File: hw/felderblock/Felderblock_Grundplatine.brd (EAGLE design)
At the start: 100 x 78 mm, 54 parts, among them IC2 LM2936, IC3 ULN2803, IC4 MCP2300X/P, J1 RJ11, J2 RJ11, M1 ARDUINO-NANO-3.0, T2 BC337, X1 TASTENSPERRE1, X2 TASTENSPERRE2, X3 SCHL-SPERRE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

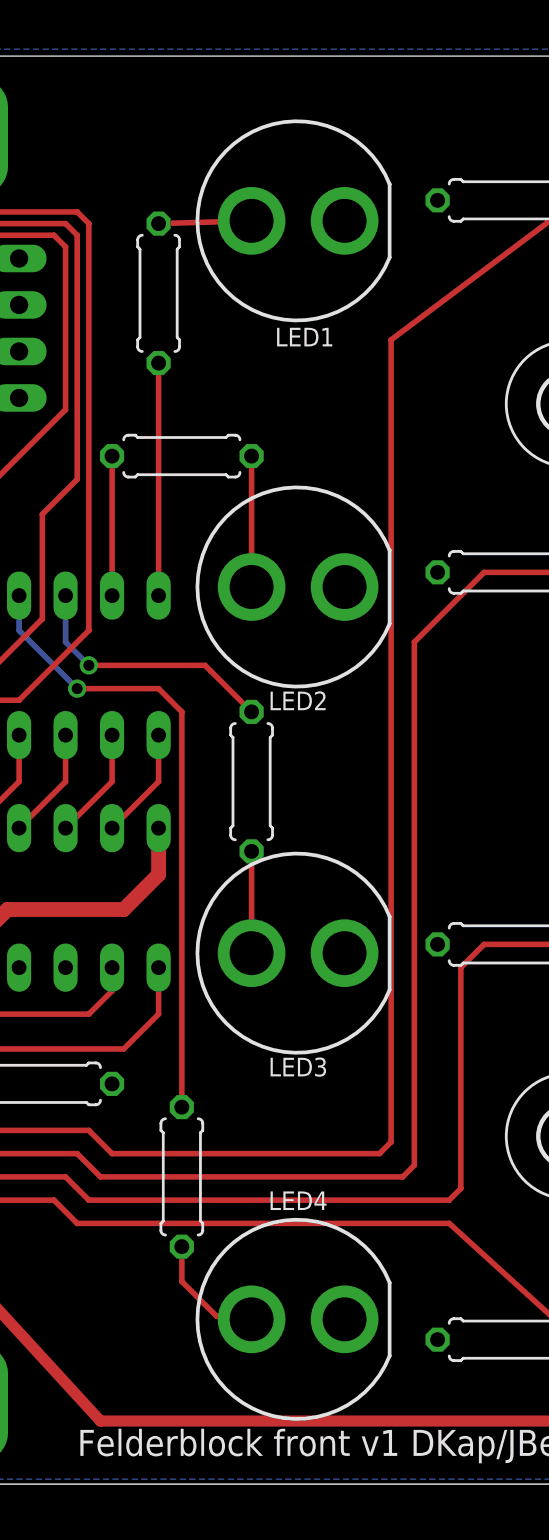
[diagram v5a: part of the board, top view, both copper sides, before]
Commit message: LED 10mm updated
changes:
- footprint 10mm LED
- INT not connected to GND (=output)
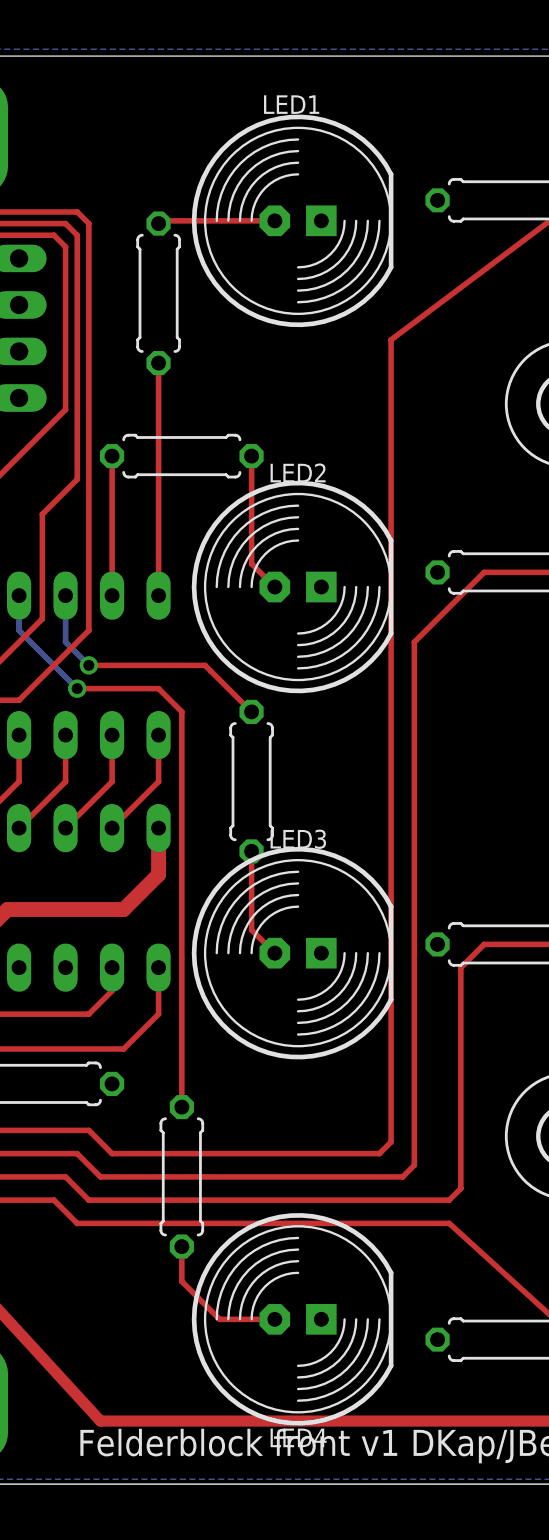
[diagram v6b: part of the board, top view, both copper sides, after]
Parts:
- LED1, LED2, LED3, LED4: device SparkFun-LED:LED_10MM -> led:LED10MM
- turned LED1 to 0 degrees
- turned LED2 to 0 degrees
- turned LED3 to 0 degrees
- turned LED4 to 0 degrees
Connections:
- removed net N$19: IC3.8
- removed net N$27: IC3.11
- net GND: now also LED1.K, LED2.K, LED3.K, LED4.K; no longer IC4.8, LED1.C, LED2.C, LED3.C, LED4.C
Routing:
- net N$4: track 5.08 -> 6.41 mm
- net N$9: track 6.51 -> 7.84 mm
- net N$8: track 5.56 -> 6.09 mm
- net N$5: track 7.15 -> 7.68 mm
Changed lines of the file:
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@@
 <attribute name="SF_ID" value="PRT_10877" x="6.35" y="54.61" size="1.778" layer="28" rot="MR0" display="off"/>
 </element>
-<element name="LED1" library="SparkFun-LED" package="LED_10MM" value="" x="76.2" y="70" smashed="yes" rot="R180">
-<attribute name="NAME" x="74.93" y="63.65" size="1.016" layer="25" ratio="20" rot="R180" align="center-right"/>
-<attribute name="VALUE" x="76.2" y="75.715" size="0.6096" layer="27" font="vector" ratio="20" rot="R180" align="top-center"/>
-</element>
-<element name="LED2" library="SparkFun-LED" package="LED_10MM" value="" x="76.2" y="50" smashed="yes" rot="R180">
-<attribute name="NAME" x="76.2" y="44.285" size="1.016" layer="25" ratio="20" rot="R180" align="bottom-center"/>
-<attribute name="VALUE" x="76.2" y="55.715" size="0.6096" layer="27" font="vector" ratio="20" rot="R180" align="top-center"/>
-</element>
-<element name="LED3" library="SparkFun-LED" package="LED_10MM" value="" x="76.2" y="30" smashed="yes" rot="R180">
-<attribute name="NAME" x="76.2" y="24.285" size="1.016" layer="25" ratio="20" rot="R180" align="bottom-center"/>
-<attribute name="VALUE" x="76.2" y="35.715" size="0.6096" layer="27" font="vector" ratio="20" rot="R180" align="top-center"/>
-</element>
-<element name="LED4" library="SparkFun-LED" package="LED_10MM" value="" x="76.2" y="10" smashed="yes" rot="R180">
-<attribute name="NAME" x="76.2" y="16.985" size="1.016" layer="25" ratio="20" rot="R180" align="bottom-center"/>
-<attribute name="VALUE" x="76.2" y="15.715" size="0.6096" layer="27" font="vector" ratio="20" rot="R180" align="top-center"/>
+<element name="LED1" library="led" package="LED10MM" value="" x="76.2" y="70" smashed="yes">
+<attribute name="NAME" x="77.47" y="76.35" size="1.016" layer="25" ratio="20" align="center-right"/>
+<attribute name="VALUE" x="76.2" y="64.285" size="0.6096" layer="27" font="vector" ratio="20" align="top-center"/>
+</element>
+<element name="LED2" library="led" package="LED10MM" value="" x="76.2" y="50" smashed="yes">
+<attribute name="NAME" x="76.2" y="55.715" size="1.016" layer="25" ratio="20" align="bottom-center"/>
+<attribute name="VALUE" x="76.2" y="44.285" size="0.6096" layer="27" font="vector" ratio="20" align="top-center"/>
+</element>
+<element name="LED3" library="led" package="LED10MM" value="" x="76.2" y="30" smashed="yes">
+<attribute name="NAME" x="76.2" y="35.715" size="1.016" layer="25" ratio="20" align="bottom-center"/>
+<attribute name="VALUE" x="76.2" y="24.285" size="0.6096" layer="27" font="vector" ratio="20" align="top-center"/>
+</element>
+<element name="LED4" library="led" package="LED10MM" value="" x="76.2" y="10" smashed="yes">
+<attribute name="NAME" x="76.2" y="3.015" size="1.016" layer="25" ratio="20" align="bottom-center"/>
+<attribute name="VALUE" x="76.2" y="4.285" size="0.6096" layer="27" font="vector" ratio="20" align="top-center"/>
 </element>
 <element name="M1" library="diy-modules" package="ARDUINO-NANO-3.0" value="ARDUINO-NANO-3.0" x="35.56" y="34.29" smashed="yes" rot="MR90"/>
@@
 <contactref element="R8" pad="2"/>
 <contactref element="R7" pad="2"/>
-<contactref element="LED4" pad="C"/>
-<contactref element="LED3" pad="C"/>
-<contactref element="LED2" pad="C"/>
-<contactref element="LED1" pad="C"/>
+<contactref element="LED4" pad="K"/>
+<contactref element="LED3" pad="K"/>
+<contactref element="LED2" pad="K"/>
+<contactref element="LED1" pad="K"/>
 <contactref element="J3" pad="6"/>
 <contactref element="J3" pad="1"/>
@@
 <contactref element="IC4" pad="9"/>
 <contactref element="IC4" pad="6"/>
-<contactref element="IC4" pad="8"/>
 <wire x1="15.24" y1="71.12" x2="22.86" y2="71.12" width="0.6096" layer="1"/>
 <contactref element="I2C" pad="4"/>
@@
 <contactref element="R11" pad="2"/>
 <contactref element="LED1" pad="A"/>
-<wire x1="68.58" y1="69.85" x2="73.66" y2="70" width="0.3048" layer="1"/>
+<wire x1="74.93" y1="70" x2="68.73" y2="70" width="0.3048" layer="1"/>
+<wire x1="68.73" y1="70" x2="68.58" y2="69.85" width="0.3048" layer="1"/>
 </signal>
 <signal name="N$5">
 <contactref element="R12" pad="2"/>
 <contactref element="LED2" pad="A"/>
-<wire x1="73.66" y1="50" x2="73.66" y2="57.15" width="0.3048" layer="1"/>
+<wire x1="73.66" y1="57.15" x2="73.66" y2="51.27" width="0.3048" layer="1"/>
+<wire x1="73.66" y1="51.27" x2="74.93" y2="50" width="0.3048" layer="1"/>
 </signal>
 <signal name="N$8">
 <contactref element="R13" pad="2"/>
 <contactref element="LED3" pad="A"/>
-<wire x1="73.66" y1="30" x2="73.66" y2="35.56" width="0.3048" layer="1"/>
+<wire x1="73.66" y1="35.56" x2="73.66" y2="31.27" width="0.3048" layer="1"/>
+<wire x1="73.66" y1="31.27" x2="74.93" y2="30" width="0.3048" layer="1"/>
 </signal>
 <signal name="N$9">
@@
 <contactref element="LED4" pad="A"/>
 <wire x1="69.85" y1="13.97" x2="69.85" y2="12.065" width="0.3048" layer="1"/>
-<wire x1="69.85" y1="12.065" x2="71.755" y2="10.16" width="0.3048" layer="1"/>
-<wire x1="71.755" y1="10.16" x2="73.66" y2="10" width="0.3048" layer="1"/>
+<wire x1="74.93" y1="10" x2="71.915" y2="10" width="0.3048" layer="1"/>
+<wire x1="71.915" y1="10" x2="69.85" y2="12.065" width="0.3048" layer="1"/>
 </signal>
 <signal name="FELD1_LED">
@@
 <wire x1="46.99" y1="65.405" x2="43.18" y2="65.405" width="0.3048" layer="1"/>
 </signal>
-<signal name="N$19">
-<contactref element="IC3" pad="8"/>
-</signal>
-<signal name="N$27">
-<contactref element="IC3" pad="11"/>
-</signal>
 <signal name="MI_FWD">
